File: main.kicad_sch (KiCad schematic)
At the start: 21 parts, among them J1 Conn_01x01_Female, J2 Conn_01x01_Female, J3 Conn_01x01_Female, J4 Conn_01x01_Female, J5 Conn_01x01_Female, J6 Conn_01x01_Female, J7 Conn_Coaxial, Q1 AOT2618

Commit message: Added BOM
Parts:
- added N1: Housing, symbol Mechanical:Housing
- C1: symbol Device:CP -> Device:C_Polarized; Alternative (none) -> United Chemicon EKYB101ELL102MM40S
- C2: Alternative (none) -> TDK CNC6P1X7R2A475K250AE; PN CNC6P1X7R2A475K250AE -> CNA6P1X7R2A475K250AE
- C3: symbol Device:CP -> Device:C_Polarized
- C4, C6: Alternative (none) -> TDK CGA5L2X7R2A105K160AA
- C5: symbol Device:C -> Device:C_Polarized; Alternative (none) -> Rubycon 160LEX33MEFC10X16; MFN Rubycon -> United Chemicon; PN 160LEX33MEFC10X16 -> EGXF351ELL330MJ35S
- LOGO1, LOGO2: now left out of the parts list
- R1: Alternative (none) -> Panasonic ERJ-6ENF1002V; MFN (none) -> Yageo; PN (none) -> AC0805FR-0710KL
- R2, R3, R4: Alternative (none) -> Panasonic ERJ-U08F49R9V; MFN Susumu -> Yageo; PN RG3216P-49R9-B-T5 -> AC1206FR-0749R9L
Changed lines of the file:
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@@
   )
   (symbol (lib_id "Graphic:Logo_Open_Hardware_Small") (at 274.32 173.99 0) (unit 1)
-    (in_bom yes) (on_board yes)
+    (in_bom no) (on_board yes)
     (property "Reference" "LOGO2" (id 0) (at 274.32 167.005 0)
       (effects (font (size 1.27 1.27)) hide)
@@
   )
   (symbol (lib_id "Custom_logos:Logo_APQ") (at 242.57 171.45 0) (unit 1)
-    (in_bom yes) (on_board yes)
+    (in_bom no) (on_board yes)
     (property "Reference" "LOGO1" (id 0) (at 248.92 164.465 0)
       (effects (font (size 1.27 1.27)) hide)
@@
     (pin "1")
   )
-  (symbol (lib_id "Device:C") (at 109.22 45.72 0) (unit 1)
+  (symbol (lib_id "Device:C_Polarized") (at 109.22 45.72 0) (unit 1)
     (in_bom yes) (on_board yes)
     (property "Reference" "C5" (id 0) (at 113.03 44.45 0)
@@
       (effects (font (size 1.27 1.27)) hide)
     )
-    (property "MFN" "Rubycon" (id 4) (at 109.22 45.72 0)
-      (effects (font (size 1.27 1.27)) hide)
-    )
-    (property "PN" "160LEX33MEFC10X16" (id 5) (at 109.22 45.72 0)
+    (property "MFN" "United Chemicon" (id 4) (at 109.22 45.72 0)
+      (effects (font (size 1.27 1.27)) hide)
+    )
+    (property "PN" "EGXF351ELL330MJ35S" (id 5) (at 109.22 45.72 0)
+      (effects (font (size 1.27 1.27)) hide)
+    )
+    (property "Alternative" "Rubycon 160LEX33MEFC10X16" (id 6) (at 109.22 45.72 0)
       (effects (font (size 1.27 1.27)) hide)
     )
@@
       (effects (font (size 1.27 1.27)) hide)
     )
-    (property "PN" "CNC6P1X7R2A475K250AE" (id 5) (at 120.65 45.72 0)
+    (property "PN" "CNA6P1X7R2A475K250AE" (id 5) (at 120.65 45.72 0)
+      (effects (font (size 1.27 1.27)) hide)
+    )
+    (property "Alternative" "TDK CNC6P1X7R2A475K250AE" (id 6) (at 120.65 45.72 0)
       (effects (font (size 1.27 1.27)) hide)
     )
@@
       (effects (font (size 1.27 1.27)) hide)
     )
+    (property "MFN" "Yageo" (id 4) (at 158.75 58.42 0)
+      (effects (font (size 1.27 1.27)) hide)
+    )
+    (property "PN" "AC0805FR-0710KL" (id 5) (at 158.75 58.42 0)
+      (effects (font (size 1.27 1.27)) hide)
+    )
+    (property "Alternative" "Panasonic ERJ-6ENF1002V" (id 6) (at 158.75 58.42 0)
+      (effects (font (size 1.27 1.27)) hide)
+    )
     (pin "1")
     (pin "2")
@@
       (effects (font (size 1.27 1.27)) hide)
     )
+    (property "Alternative" "TDK CGA5L2X7R2A105K160AA" (id 6) (at 148.59 81.28 0)
+      (effects (font (size 1.27 1.27)) hide)
+    )
     (pin "1")
     (pin "2")
@@
     )
     (property "PN" "CGA5L2X7R2A105M160AE" (id 5) (at 158.75 81.28 0)
+      (effects (font (size 1.27 1.27)) hide)
+    )
+    (property "Alternative" "TDK CGA5L2X7R2A105K160AA" (id 6) (at 158.75 81.28 0)
       (effects (font (size 1.27 1.27)) hide)
     )
@@
       (effects (font (size 1.27 1.27)) hide)
     )
-    (property "MFN" "Susumu" (id 4) (at 118.11 99.06 0)
-      (effects (font (size 1.27 1.27)) hide)
-    )
-    (property "PN" "RG3216P-49R9-B-T5" (id 5) (at 118.11 99.06 0)
+    (property "MFN" "Yageo" (id 4) (at 118.11 99.06 0)
+      (effects (font (size 1.27 1.27)) hide)
+    )
+    (property "PN" "AC1206FR-0749R9L" (id 5) (at 118.11 99.06 0)
+      (effects (font (size 1.27 1.27)) hide)
+    )
+    (property "Alternative" "Panasonic ERJ-U08F49R9V" (id 6) (at 118.11 99.06 0)
       (effects (font (size 1.27 1.27)) hide)
     )
@@
     (pin "1")
   )
-  (symbol (lib_id "Device:CP") (at 201.93 55.88 0) (unit 1)
+  (symbol (lib_id "Device:C_Polarized") (at 201.93 55.88 0) (unit 1)
     (in_bom yes) (on_board yes)
     (property "Reference" "C1" (id 0) (at 205.74 54.61 0)
@@
       (effects (font (size 1.27 1.27)) hide)
     )
-    (pin "1")
-    (pin "2")
-  )
-  (symbol (lib_id "Device:CP") (at 201.93 118.11 0) (unit 1)
+    (property "Alternative" "United Chemicon EKYB101ELL102MM40S" (id 6) (at 201.93 55.88 0)
+      (effects (font (size 1.27 1.27)) hide)
+    )
+    (pin "1")
+    (pin "2")
+  )
+  (symbol (lib_id "Device:C_Polarized") (at 201.93 118.11 0) (unit 1)
     (in_bom yes) (on_board yes)
     (property "Reference" "C3" (id 0) (at 205.74 116.84 0)
@@
       (effects (font (size 1.27 1.27)) hide)
     )
-    (property "MFN" "Susumu" (id 4) (at 201.93 66.04 0)
-      (effects (font (size 1.27 1.27)) hide)
-    )
-    (property "PN" "RG3216P-49R9-B-T5" (id 5) (at 201.93 66.04 0)
+    (property "MFN" "Yageo" (id 4) (at 201.93 66.04 0)
+      (effects (font (size 1.27 1.27)) hide)
+    )
+    (property "PN" "AC1206FR-0749R9L" (id 5) (at 201.93 66.04 0)
+      (effects (font (size 1.27 1.27)) hide)
+    )
+    (property "Alternative" "Panasonic ERJ-U08F49R9V" (id 6) (at 201.93 66.04 0)
       (effects (font (size 1.27 1.27)) hide)
     )
@@
       (effects (font (size 1.27 1.27)) hide)
     )
-    (property "MFN" "Susumu" (id 4) (at 201.93 107.95 0)
-      (effects (font (size 1.27 1.27)) hide)
-    )
-    (property "PN" "RG3216P-49R9-B-T5" (id 5) (at 201.93 107.95 0)
+    (property "MFN" "Yageo" (id 4) (at 201.93 107.95 0)
+      (effects (font (size 1.27 1.27)) hide)
+    )
+    (property "PN" "AC1206FR-0749R9L" (id 5) (at 201.93 107.95 0)
+      (effects (font (size 1.27 1.27)) hide)
+    )
+    (property "Alternative" "Panasonic ERJ-U08F49R9V" (id 6) (at 201.93 107.95 0)
       (effects (font (size 1.27 1.27)) hide)
     )
@@
     )
     (pin "1")
+  )
+  (symbol (lib_id "Mechanical:Housing") (at 55.88 40.005 0) (unit 1)
+    (in_bom yes) (on_board no) (fields_autoplaced)
+    (property "Reference" "N1" (id 0) (at 59.69 39.0524 0)
+      (effects (font (size 1.27 1.27)) (justify left))
+    )
+    (property "Value" "Housing" (id 1) (at 59.69 41.5924 0)
+      (effects (font (size 1.27 1.27)) (justify left))
+    )
+    (property "Footprint" "" (id 2) (at 57.15 38.735 0)
+      (effects (font (size 1.27 1.27)) hide)
+    )
+    (property "Datasheet" "~" (id 3) (at 57.15 38.735 0)
+      (effects (font (size 1.27 1.27)) hide)
+    )
+    (property "MFN" "Hammond Manufacturing Ltd." (id 4) (at 55.88 40.005 0)
+      (effects (font (size 1.27 1.27)) hide)
+    )
+    (property "PN" "1457N1201EBK" (id 5) (at 55.88 40.005 0)
+      (effects (font (size 1.27 1.27)) hide)
+    )
   )
   (sheet_instances
@@
       (reference "LOGO2") (unit 1) (value "Logo_Open_Hardware_Small") (footprint "Symbol:OSHW-Logo_7.5x8mm_SilkScreen")
     )
+    (path "/689f734d-c5fd-4493-889a-b9878aa9fd1f"
+      (reference "N1") (unit 1) (value "Housing") (footprint "")
+    )
     (path "/00000000-0000-0000-0000-0000618e1cab"

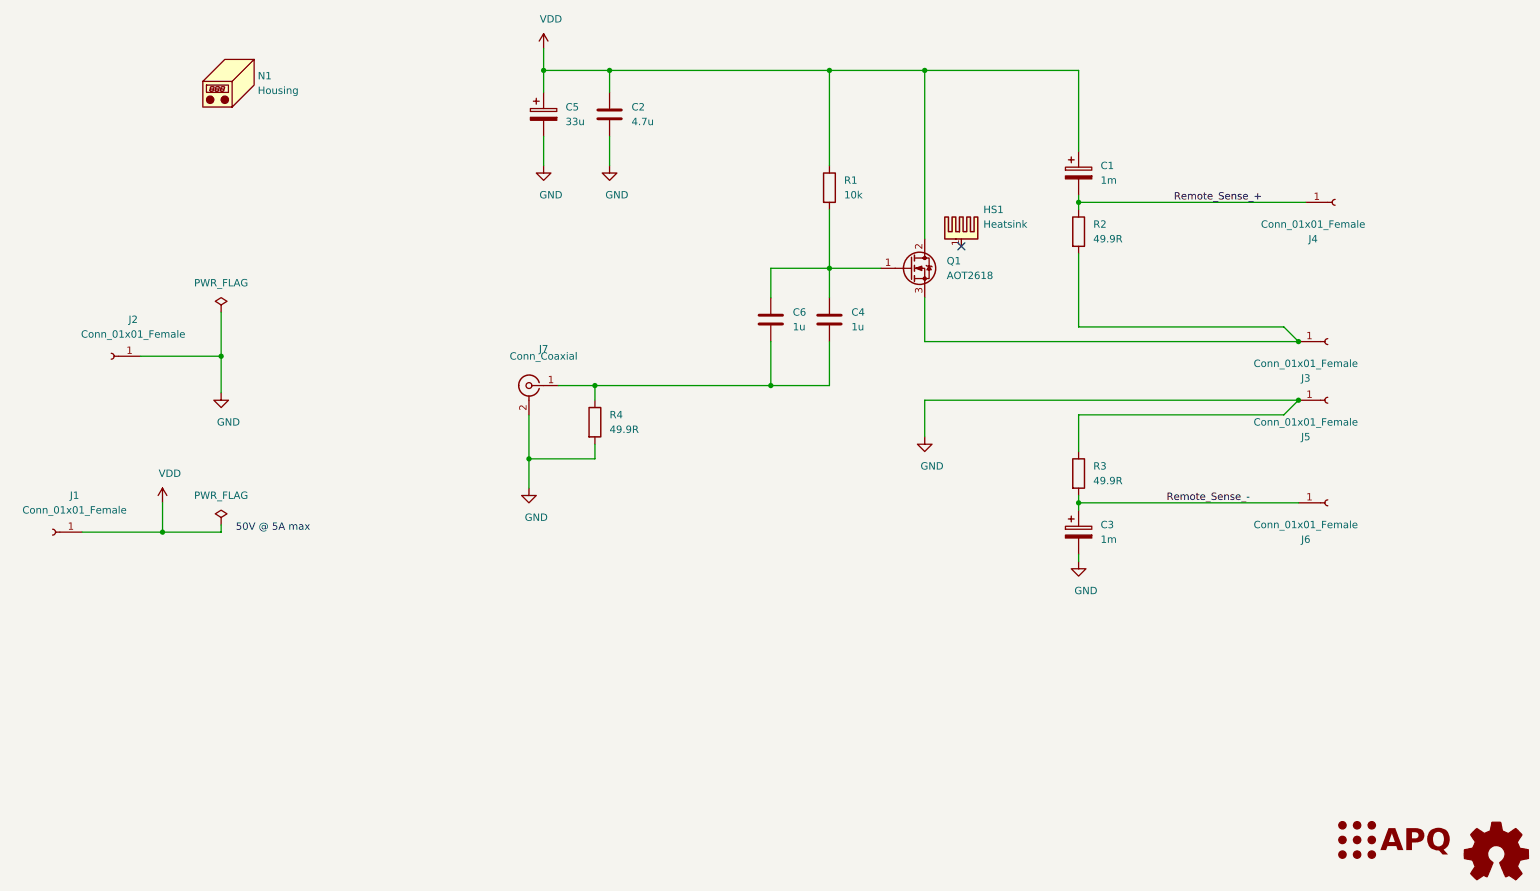
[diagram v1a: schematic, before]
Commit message: Update to KiCad 8
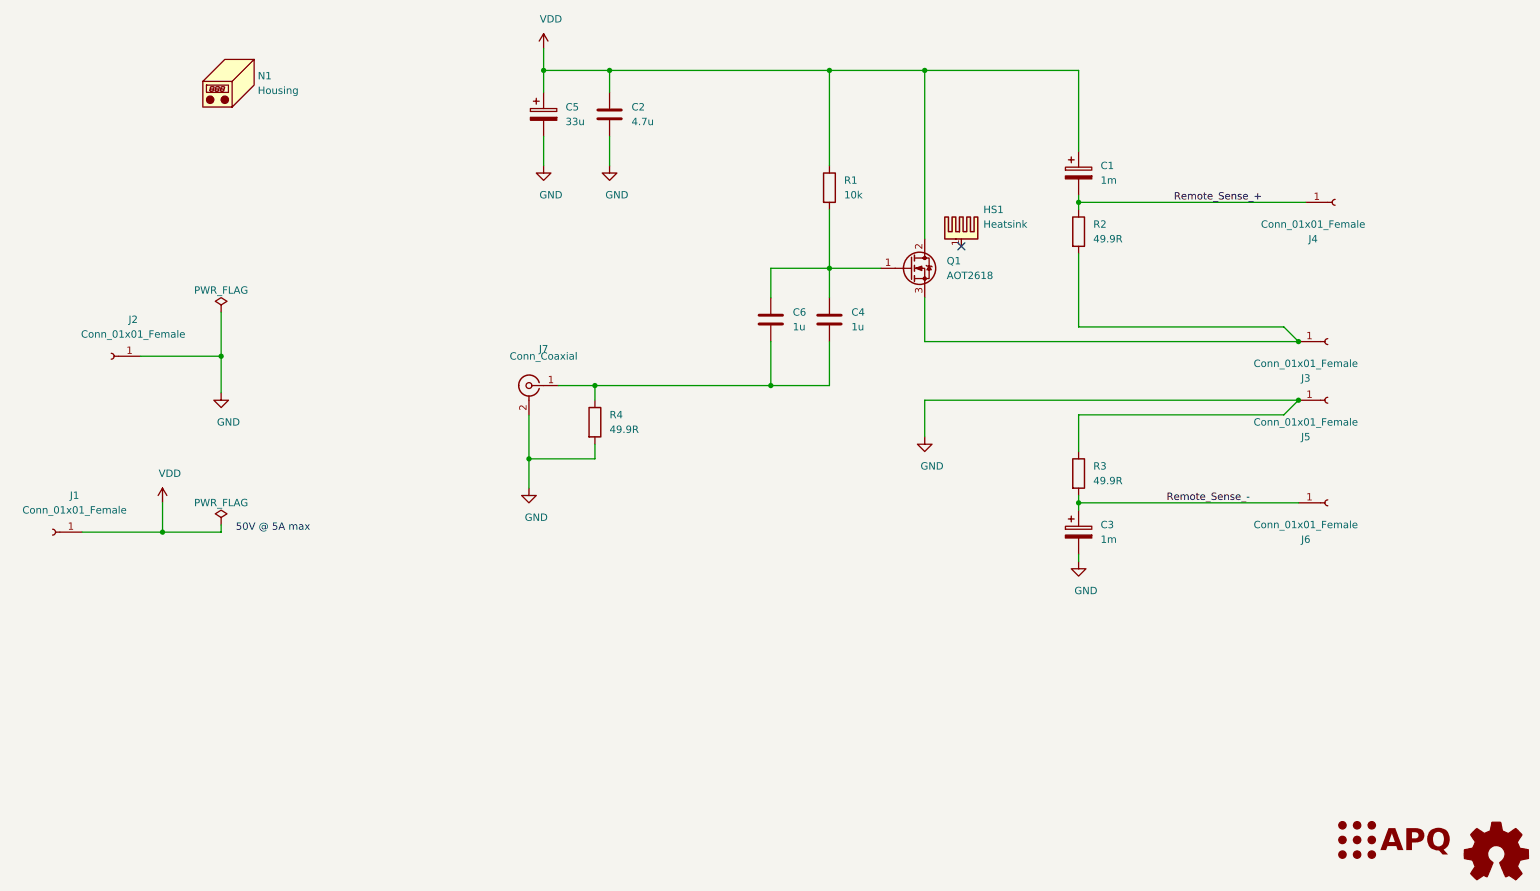
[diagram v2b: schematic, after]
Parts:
- J1, J3, J4: footprint Custom_footprints:Schuetzinger_4mm_Jack -> Connector:Banana_Cliff_FCR7350R_S16N-PC_Horizontal; symbol Connector:Conn_01x01_Female -> Connector:Conn_01x01_Socket
- J2, J5, J6: footprint Custom_footprints:Schuetzinger_4mm_Jack -> Connector:Banana_Cliff_FCR7350B_S16N-PC_Horizontal; symbol Connector:Conn_01x01_Female -> Connector:Conn_01x01_Socket
